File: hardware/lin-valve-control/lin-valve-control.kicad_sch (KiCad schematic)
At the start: 2 parts, among them U1 Arduino_Nano_v3.x

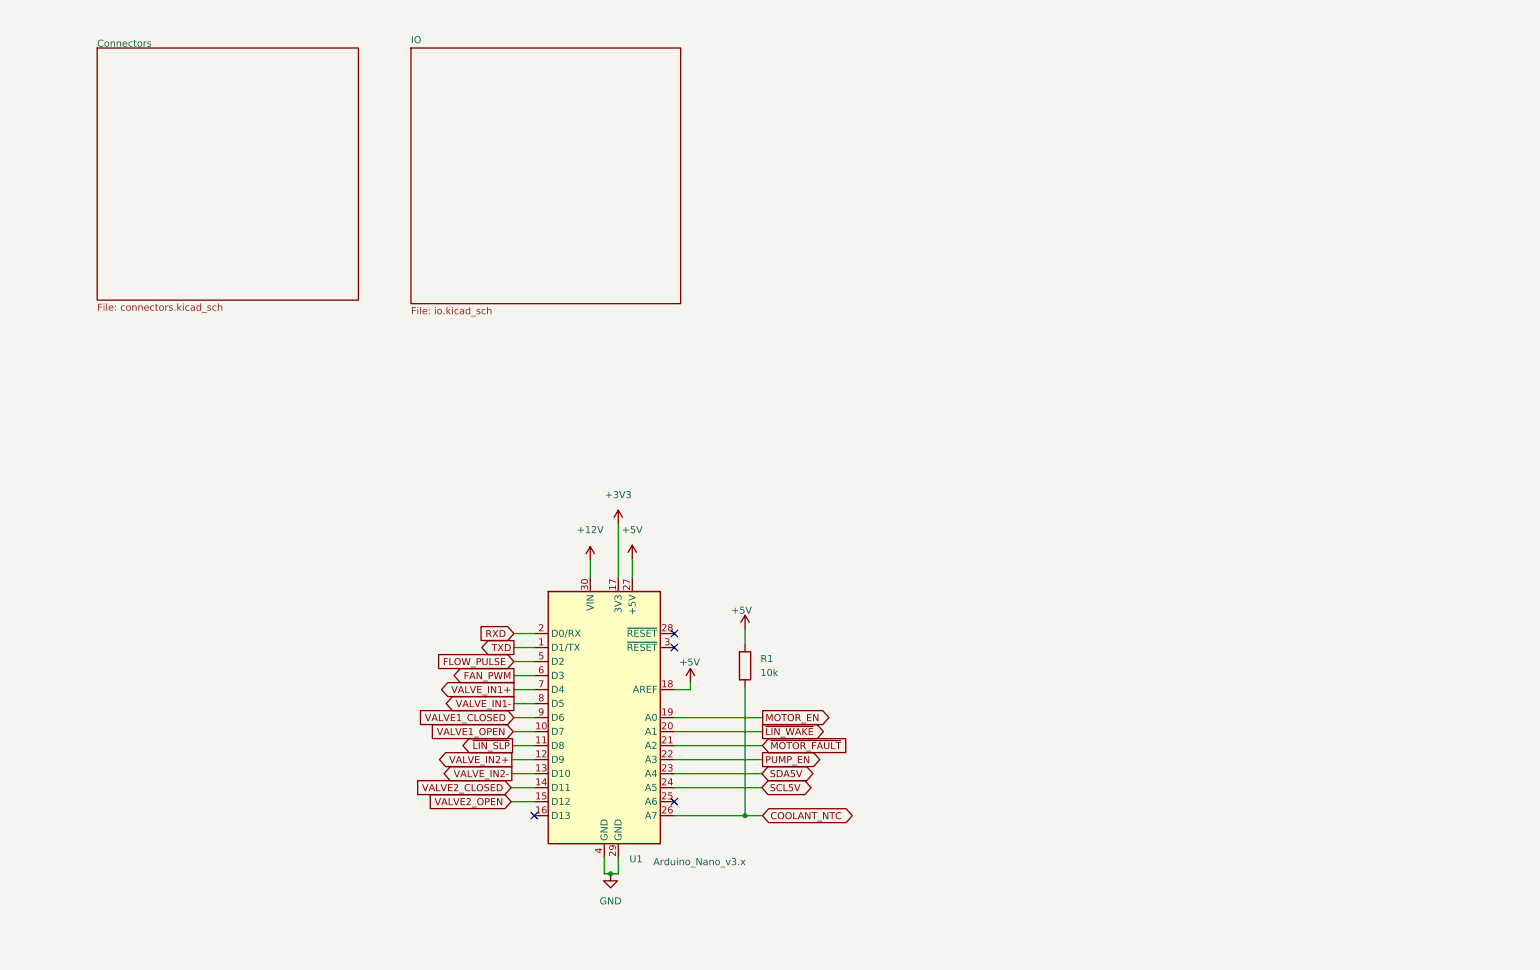
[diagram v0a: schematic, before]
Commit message: Completely redo the valve controller.  One valve only.
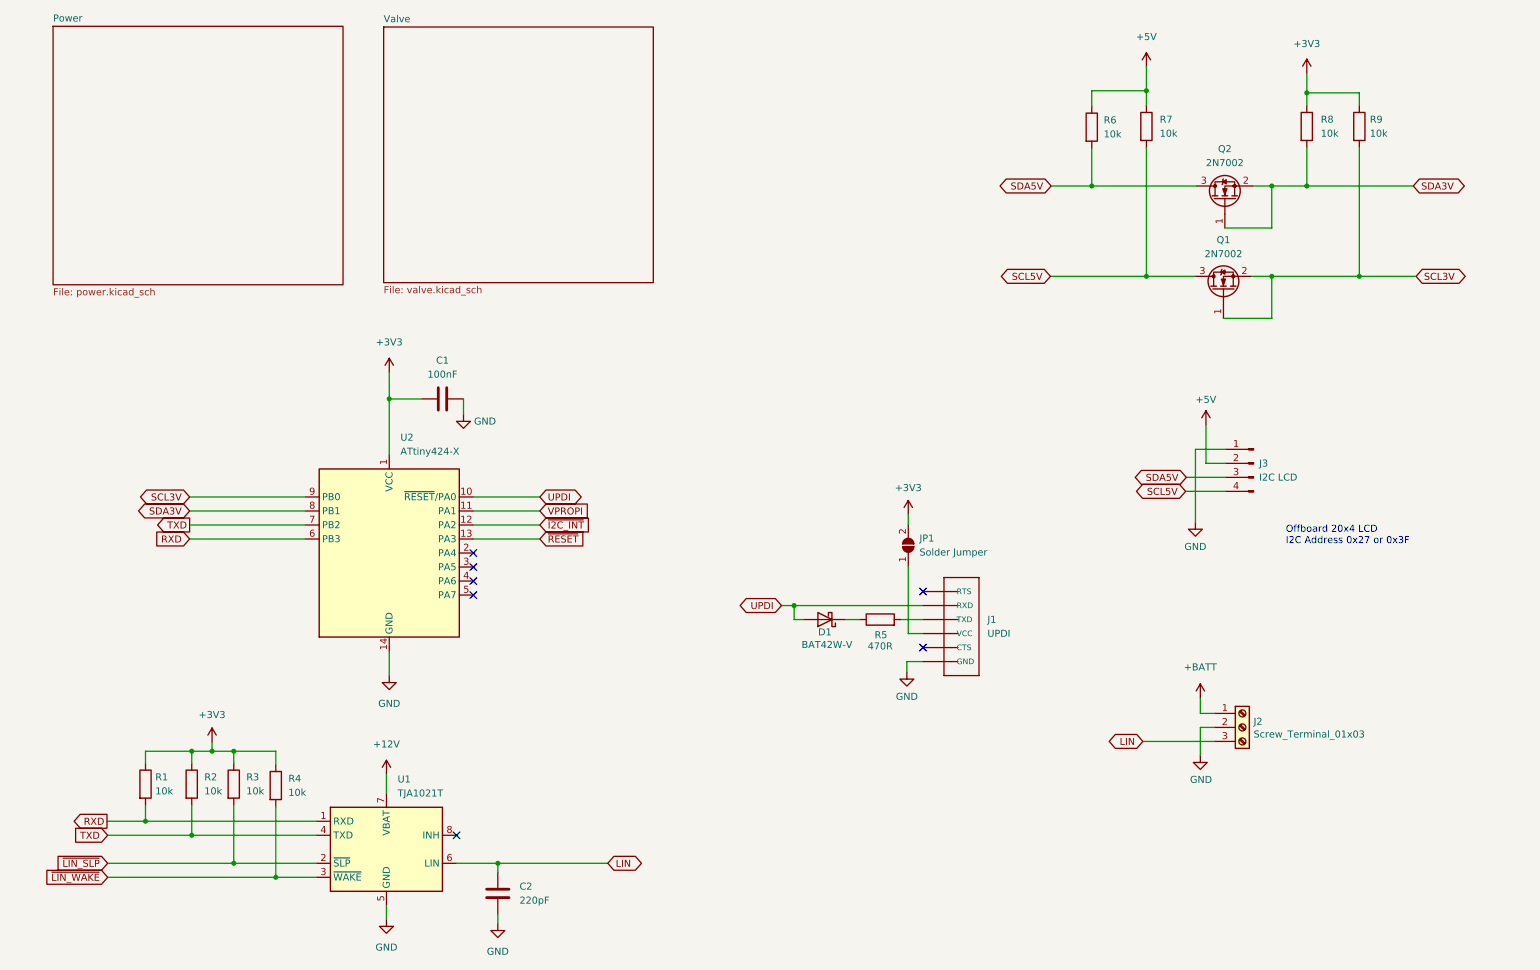
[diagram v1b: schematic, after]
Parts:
- removed U1: Arduino_Nano_v3.x, Module:Arduino_Nano, symbol MCU_Module:Arduino_Nano_v3.x
- added C1: 100nF, Capacitor_SMD:C_0805_2012Metric_Pad1.18x1.45mm_HandSolder, symbol Device:C
- added C2: 220pF, Capacitor_SMD:C_0805_2012Metric_Pad1.18x1.45mm_HandSolder, symbol Device:C
- added D1: BAT42W-V, Diode_SMD:D_SOD-123, symbol Diode:BAT42W-V
- added J1: UPDI, Beirdo:FTDI_BASIC, symbol Beirdo:FTDI_BASICPTH
- added J2: Screw_Terminal_01x03, TerminalBlock_TE-Connectivity:TerminalBlock_TE_282834-3_1x03_P2.54mm_Horizontal, symbol Connector:Screw_Terminal_01x03
- added J3: I2C LCD, Connector_PinHeader_2.54mm:PinHeader_1x04_P2.54mm_Vertical, symbol Connector:Conn_01x04_Male
- added JP1: Solder Jumper, Jumper:SolderJumper-2_P1.3mm_Open_TrianglePad1.0x1.5mm, symbol Jumper:SolderJumper_2_Open
- added Q1, Q2: 2N7002, Package_TO_SOT_SMD:SOT-23, symbol Transistor_FET:2N7002
- added R2, R3, R4, R6, R7, R8, R9: 10k, Resistor_SMD:R_0805_2012Metric_Pad1.20x1.40mm_HandSolder, symbol Device:R
- added R5: 470R, Resistor_SMD:R_0805_2012Metric_Pad1.20x1.40mm_HandSolder, symbol Device:R
- added U1: TJA1021T, Package_SO:SOIC-8_3.9x4.9mm_P1.27mm, symbol Interface_CAN_LIN:TJA1021T
- added U2: ATtiny424-X, Package_SO:TSSOP-14_4.4x5mm_P0.65mm, symbol MCU_Microchip_ATtiny:ATtiny424-X
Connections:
- net COOLANT_NTC is gone; now on net RXD: R1.2
- net +12V: now also U1.7 (VBAT)
- net +3V3: now also R1.1, C1.2, JP1.2 (B), R2.1, R3.1, R4.1, R8.1, R9.1, U2.1 (VCC)
- net +5V: now also J3.2 (Pin_2), R6.1, R7.1; no longer R1.1
- net GND: now also C1.1, C2.2, J1.1 (GND), J2.2 (Pin_2), J3.1 (Pin_1), U1.5 (GND), U2.14 (GND)
- net RXD: now also U1.1 (RXD), U2.6 (PB3)
- net SCL5V: now also J3.4 (Pin_4), Q1.3 (D), R7.2
- net SDA5V: now also J3.3 (Pin_3), Q2.3 (D), R6.2
- net TXD: now also R2.2, U1.4 (TXD), U2.7 (PB2)
- net ~{LIN_SLP}: now also R3.2, U1.2 (~{SLP})
- net ~{LIN_WAKE}: now also R4.2, U1.3 (~{WAKE})
- new net: J1.3 (VCC), JP1.1 (A)
- new net: J1.4 (TXD), R5.2
- new net: D1.1 (K), R5.1
- new net +BATT: J2.1 (Pin_1)
- new net LIN: C2.1, J2.3 (Pin_3), U1.6 (LIN)
- new net SCL3V: Q1.1 (G), Q1.2 (S), R9.2, U2.9 (PB0)
- new net SDA3V: Q2.1 (G), Q2.2 (S), R8.2, U2.8 (PB1)
- new net UPDI: D1.2 (A), J1.5 (RXD), U2.10 (~{RESET}/PA0)
- new net VPROPI: U2.11 (PA1)
- new net ~{I2C_INT}: U2.12 (PA2)
- new net ~{RESET}: U2.13 (PA3)
- no-connect marks 4 -> 7
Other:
- sheet IO renamed Valve
- removed sheet Connectors
- added sheet Power (power.kicad_sch)
- sheet Valve: file io.kicad_sch -> valve.kicad_sch
- note added: "Offboard 20x4 LCD I2C Address 0x27 or 0x3F"

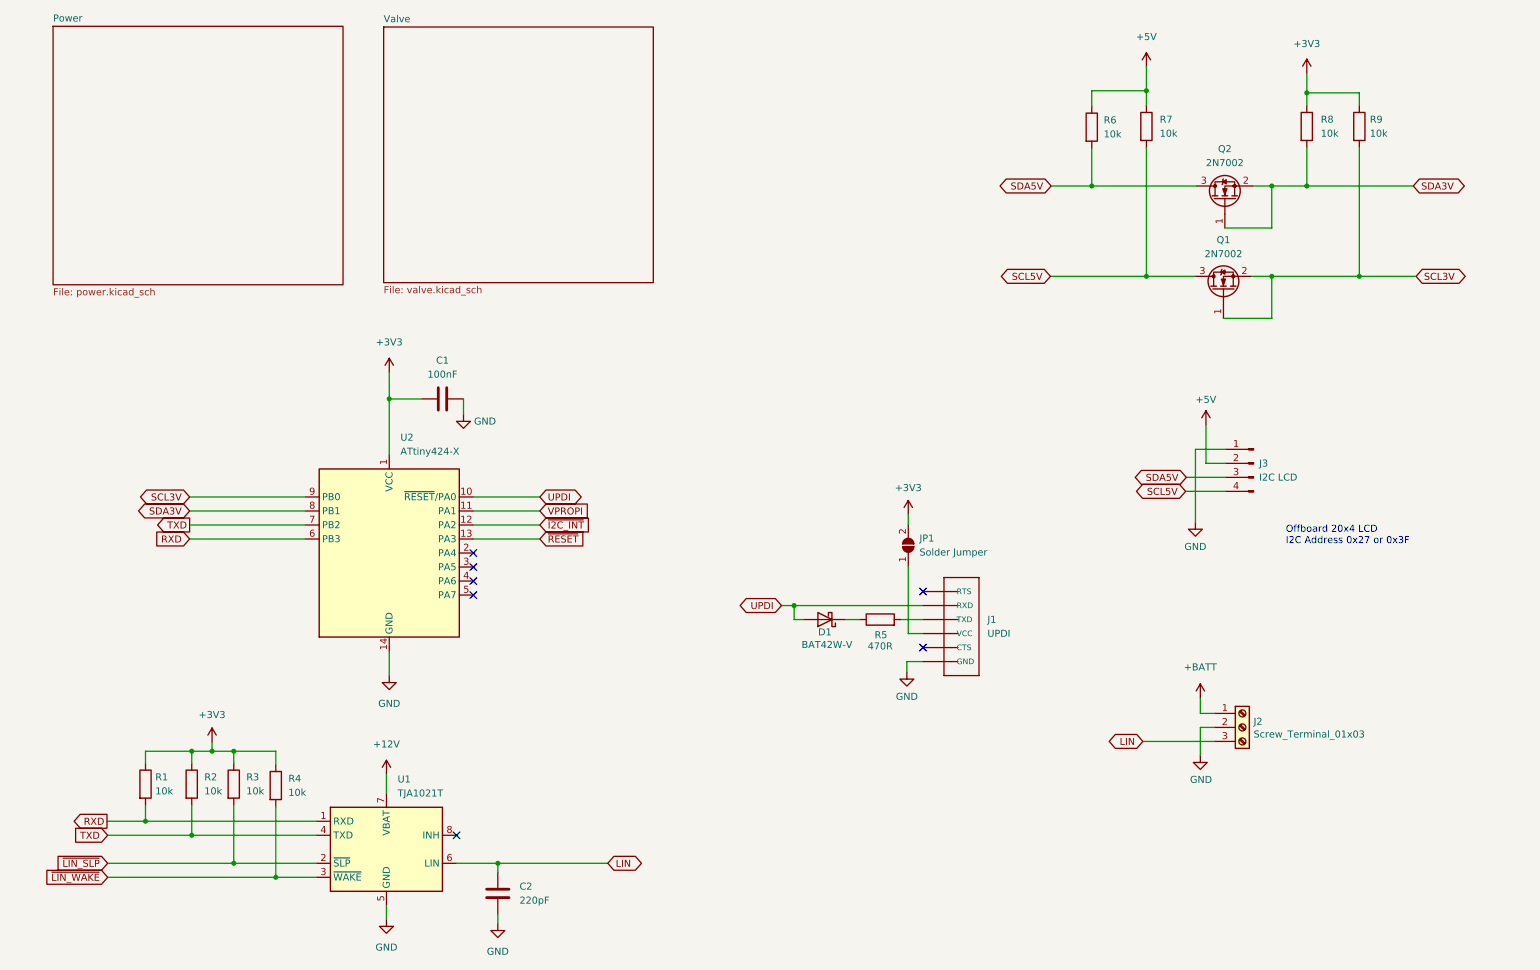
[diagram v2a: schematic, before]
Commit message: Add PCA9536 for the LINBus Address
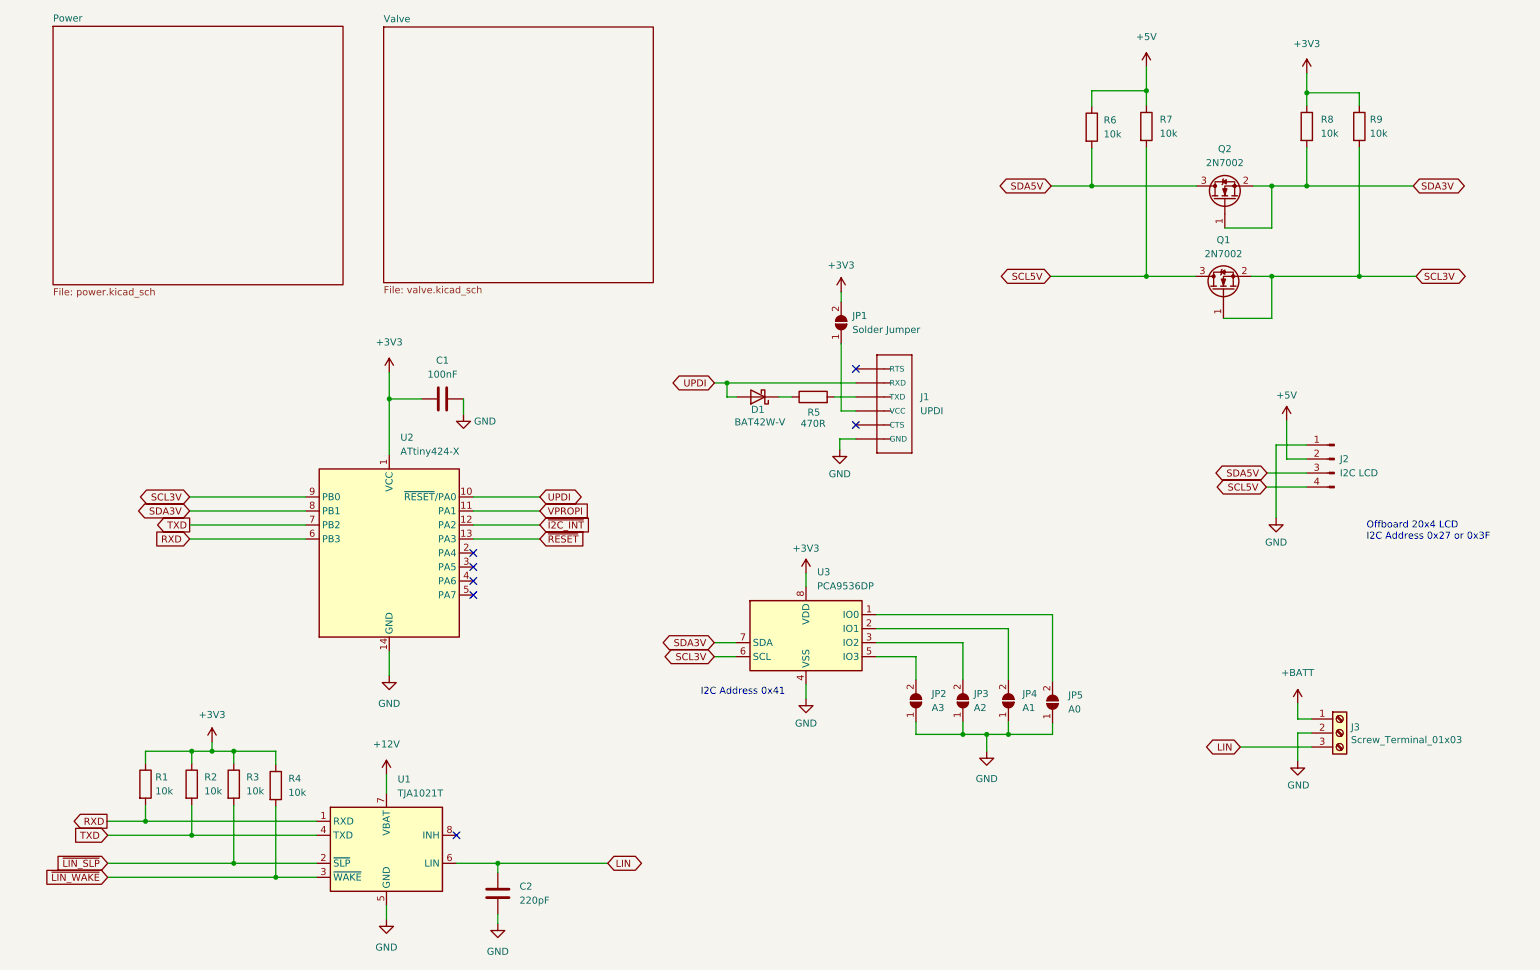
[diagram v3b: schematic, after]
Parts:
- added JP2: A3, Jumper:SolderJumper-2_P1.3mm_Open_TrianglePad1.0x1.5mm, symbol Jumper:SolderJumper_2_Open
- added JP3: A2, Jumper:SolderJumper-2_P1.3mm_Open_TrianglePad1.0x1.5mm, symbol Jumper:SolderJumper_2_Open
- added JP4: A1, Jumper:SolderJumper-2_P1.3mm_Open_TrianglePad1.0x1.5mm, symbol Jumper:SolderJumper_2_Open
- added JP5: A0, Jumper:SolderJumper-2_P1.3mm_Open_TrianglePad1.0x1.5mm, symbol Jumper:SolderJumper_2_Open
- added U3: PCA9536DP, Package_SO:TSSOP-8_3x3mm_P0.65mm, symbol Interface_Expansion:PCA9536DP
- renumbered J3 to J2, J2 to J3
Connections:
- net +3V3: now also U3.8 (VDD)
- net GND: now also JP2.1 (A), JP3.1 (A), JP4.1 (A), JP5.1 (A), U3.4 (VSS)
- net SCL3V: now also U3.6 (SCL)
- net SDA3V: now also U3.7 (SDA)
- new net: JP3.2 (B), U3.3 (IO2)
- new net: JP4.2 (B), U3.2 (IO1)
- new net: JP2.2 (B), U3.5 (IO3)
- new net: JP5.2 (B), U3.1 (IO0)
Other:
- note added: "I2C Address 0x41"
- moved on the sheet: D1, J1, J2, J3, JP1, R5

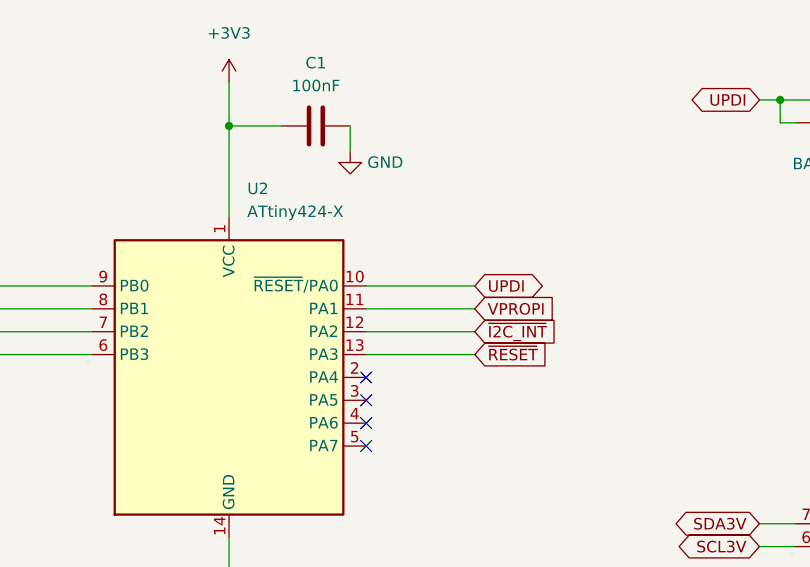
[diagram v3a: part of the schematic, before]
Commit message: Get this in place (barely) on ATTiny824.
- should not be THAT big, I thought.  Investigation to follow:

Sketch uses 7998 bytes (97%) of program storage space. Maximum is 8192 bytes.
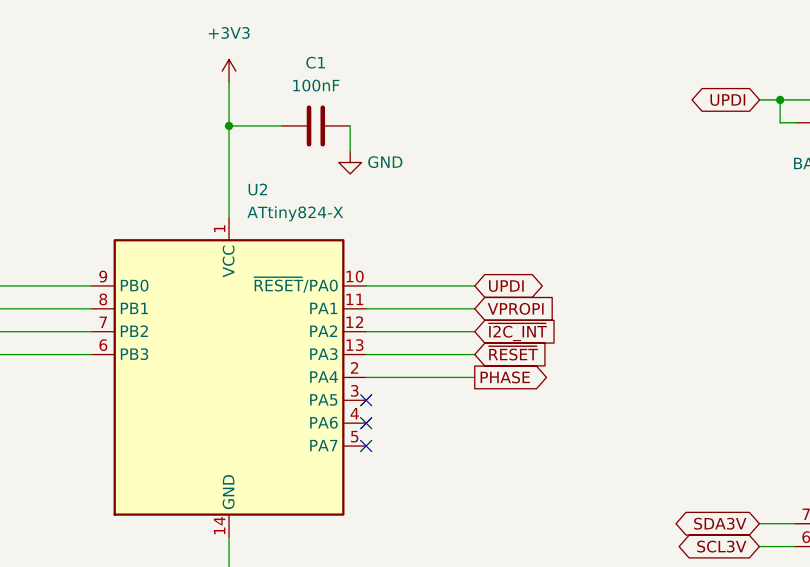
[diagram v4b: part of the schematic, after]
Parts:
- removed U2: ATtiny424-X, Package_SO:TSSOP-14_4.4x5mm_P0.65mm, symbol MCU_Microchip_ATtiny:ATtiny424-X
- added U2: ATtiny824-X, Package_SO:TSSOP-14_4.4x5mm_P0.65mm, symbol MCU_Microchip_ATtiny:ATtiny824-X
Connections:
- net +3V3: now also U2.1 (VCC)
- net GND: now also U2.14 (GND)
- net RXD: now also U2.6 (PB3)
- net SCL3V: now also U2.9 (PB0)
- net SDA3V: now also U2.8 (PB1)
- net TXD: now also U2.7 (PB2)
- net UPDI: now also U2.10 (~{RESET}/PA0)
- net VPROPI: now also U2.11 (PA1)
- net ~{I2C_INT}: now also U2.12 (PA2)
- net ~{RESET}: now also U2.13 (PA3)
- new net PHASE: U2.2 (PA4)
- no-connect marks 7 -> 6
